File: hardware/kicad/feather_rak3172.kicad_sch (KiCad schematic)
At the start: 49 parts, among them J1 Pin Header, J2 Pin Header, J3 USB_C_Receptacle_USB2.0, J4 915MHz SMA, J5 SWD, J6 JST-2PH, Q1 DMG341, SW1 RESET, SW2 BOOT, U1 RAK3172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

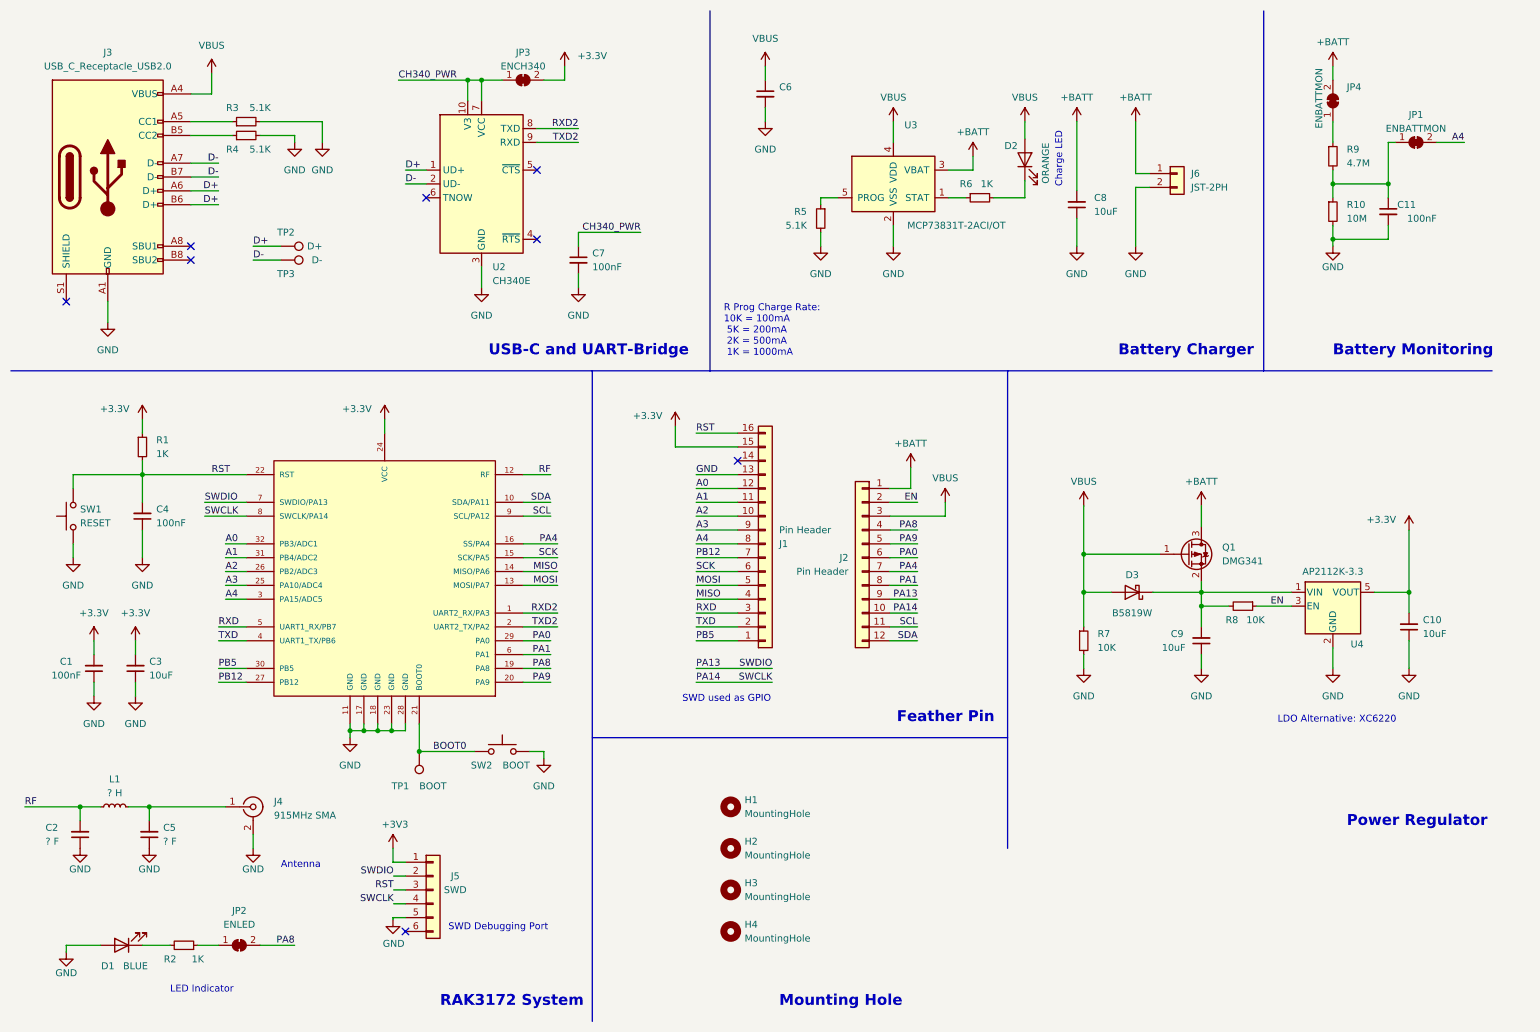
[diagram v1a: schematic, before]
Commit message: remove matching circuit, trace too short
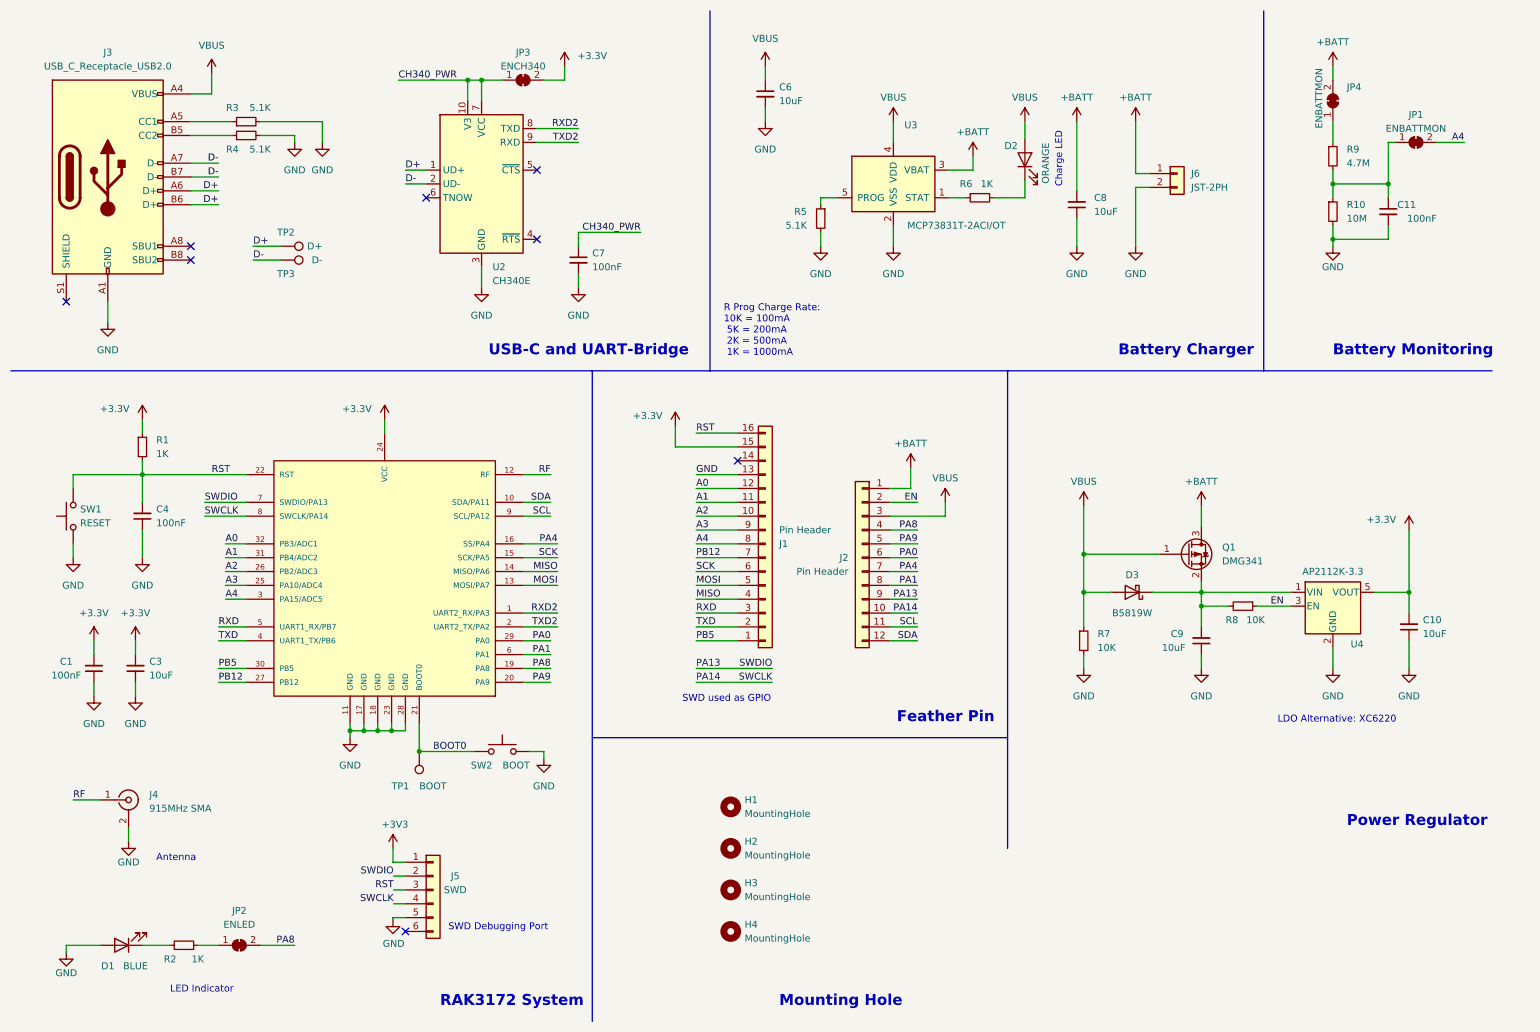
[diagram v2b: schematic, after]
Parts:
- removed C2, C5: ? F, Capacitor_SMD:C_0402_1005Metric, symbol Device:C_Small
- removed L1: ? H, Inductor_SMD:L_0402_1005Metric, symbol Device:L_Small
- C6: value (none) -> 10uF; footprint (none) -> Capacitor_SMD:C_0603_1608Metric
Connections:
- net RF: now also J4.1 (In)
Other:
- moved on the sheet: J4

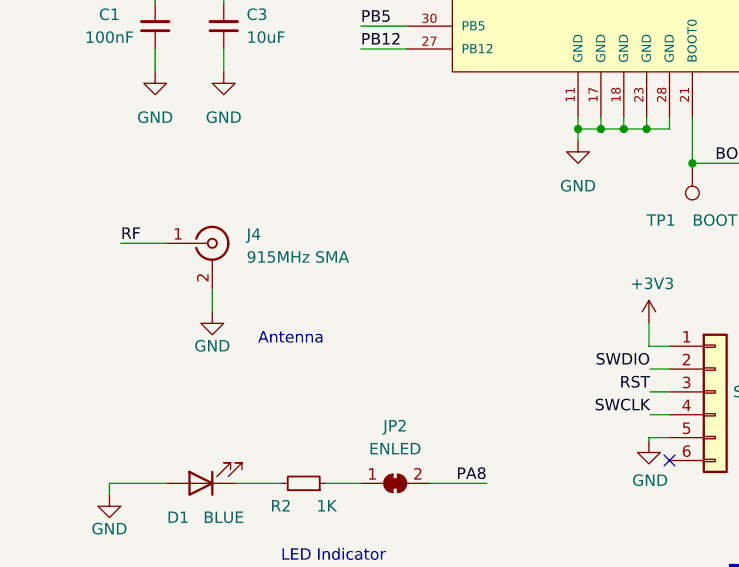
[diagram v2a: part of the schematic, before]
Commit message: re-add matching circuit, improve rf trace angle
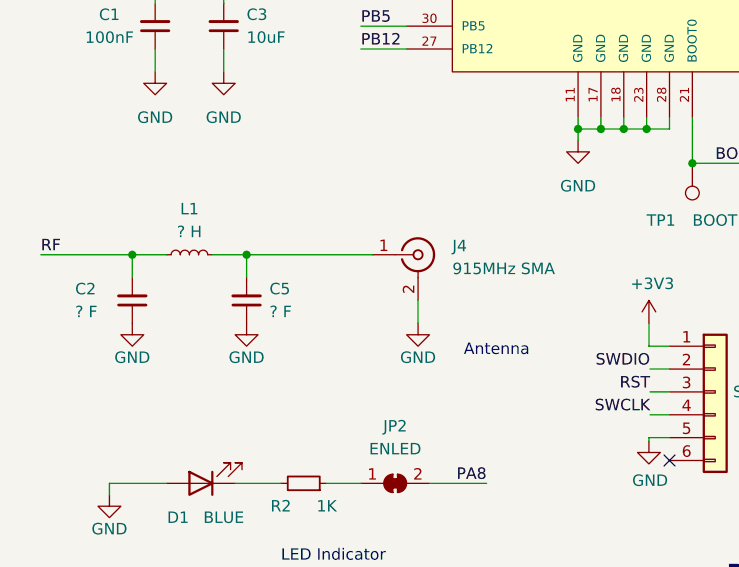
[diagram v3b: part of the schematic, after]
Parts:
- added C2, C5: ? F, Capacitor_SMD:C_0402_1005Metric, symbol Device:C_Small
- added L1: ? H, Inductor_SMD:L_0402_1005Metric, symbol Device:L_Small
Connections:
- net GND: now also C2.1, C5.1
- net RF: now also C2.2, L1.1; no longer J4.1 (In)
- new net: C5.2, J4.1 (In), L1.2
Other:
- moved on the sheet: J4

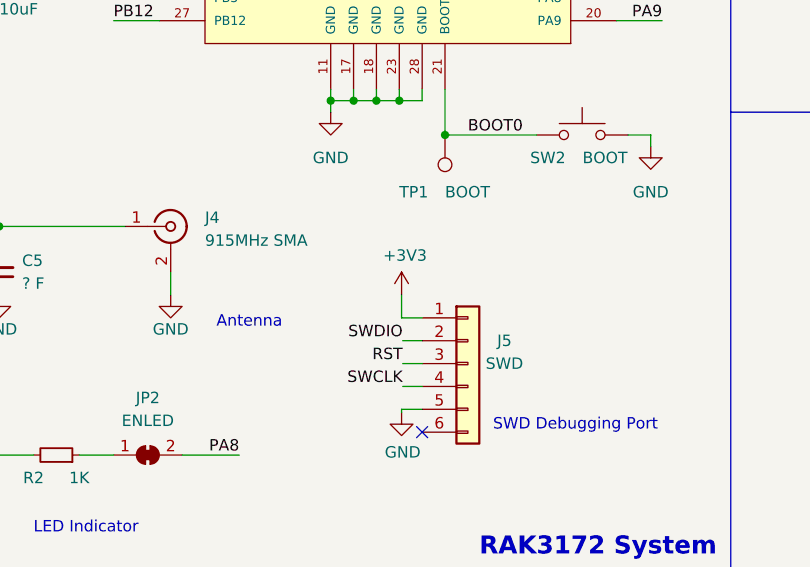
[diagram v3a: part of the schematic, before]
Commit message: remove 3v3 signal from swd pinout
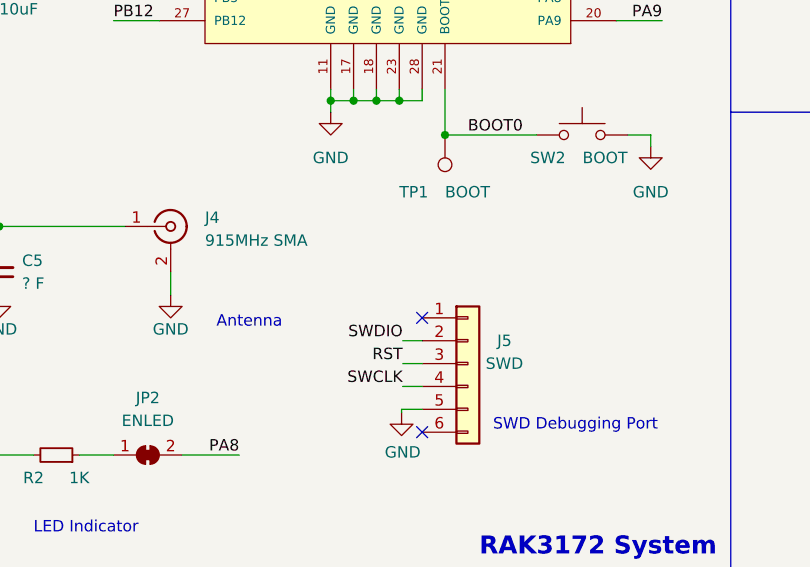
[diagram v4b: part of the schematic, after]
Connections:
- net +3V3: no longer names the net of J5.1 (Pin_1)
- no-connect marks 8 -> 9
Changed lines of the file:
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@@
   (no_connect (at 109.22 41.91))
   (no_connect (at 146.05 95.25))
+  (no_connect (at 85.09 168.91))
   (no_connect (at 88.9 46.99))
   (no_connect (at 22.86 66.04))
@@
     (stroke (width 0) (type default) (color 0 0 0 0))
   )
-  (wire (pts (xy 82.804 168.91) (xy 85.09 168.91))
-    (stroke (width 0) (type default) (color 0 0 0 0))
-  )
   (wire (pts (xy 49.53 27.94) (xy 45.72 27.94))
     (stroke (width 0) (type default) (color 0 0 0 0))
@@
   )
   (wire (pts (xy 138.43 133.35) (xy 152.4 133.35))
-    (stroke (width 0) (type default) (color 0 0 0 0))
-  )
-  (wire (pts (xy 82.804 166.37) (xy 82.804 168.91))
     (stroke (width 0) (type default) (color 0 0 0 0))
   )
@@
     (pin "2")
   )
-  (symbol (lib_id "power:+3V3") (at 82.804 166.37 0) (unit 1)
-    (in_bom yes) (on_board yes)
-    (property "Reference" "#PWR0125" (id 0) (at 82.804 170.18 0)
-      (effects (font (size 1.27 1.27)) hide)
-    )
-    (property "Value" "+3V3" (id 1) (at 83.185 161.9758 0))
-    (property "Footprint" "" (id 2) (at 82.804 166.37 0)
-      (effects (font (size 1.27 1.27)) hide)
-    )
-    (property "Datasheet" "" (id 3) (at 82.804 166.37 0)
-      (effects (font (size 1.27 1.27)) hide)
-    )
-    (pin "1")
-  )
   (symbol (lib_id "Device:R_Small") (at 190.5 46.99 90) (mirror x) (unit 1)
     (in_bom yes) (on_board yes)
@@
       (reference "#PWR0124") (unit 1) (value "GND") (footprint "")
     )
-    (path "/ec477f20-2bfc-47a1-aeed-0615d880ae23"
-      (reference "#PWR0125") (unit 1) (value "+3V3") (footprint "")
-    )
     (path "/799d7101-51e0-4b76-88e0-543d20c53ec5"

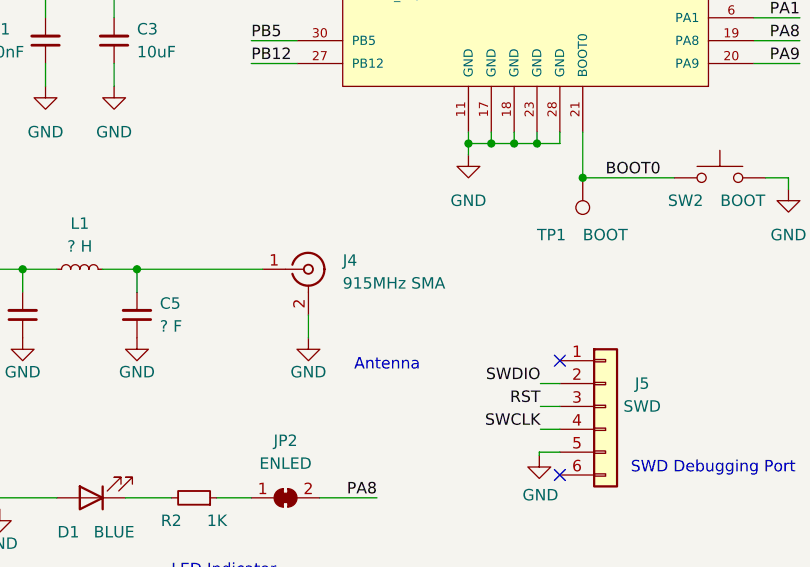
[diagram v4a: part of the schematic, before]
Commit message: change antenna part number
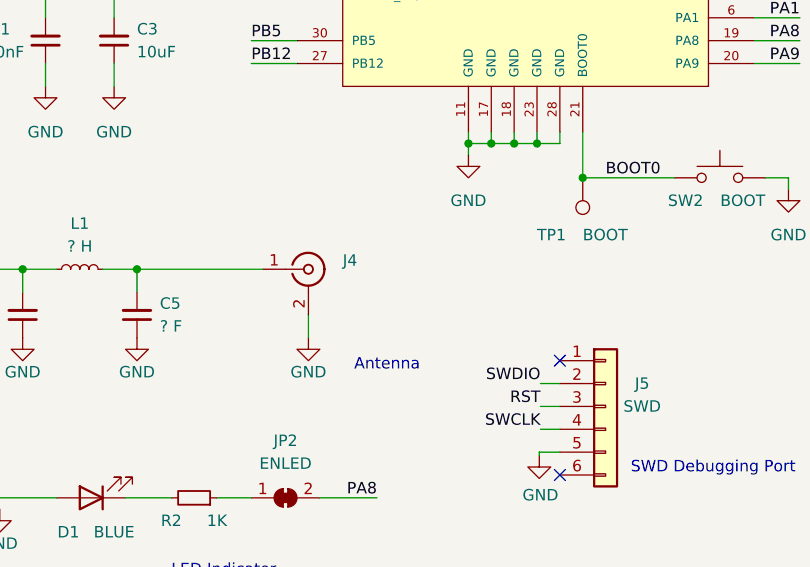
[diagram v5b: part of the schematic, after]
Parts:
- J4: value 915MHz SMA -> (none); footprint Teapot:SMA_HJTech_023 -> (none); Manufacturer HJ Tech -> DreamLNK; Part Number HJ-SMA023 -> SMA-KE-P903
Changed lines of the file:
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@@
       (effects (font (size 1.27 1.27)) (justify left))
     )
-    (property "Value" "915MHz SMA" (id 1) (at 60.96 160.3131 0)
+    (property "Value" "" (id 1) (at 60.96 160.3131 0)
       (effects (font (size 1.27 1.27)) (justify left))
     )
-    (property "Footprint" "Teapot:SMA_HJTech_023" (id 2) (at 57.15 158.75 0)
+    (property "Footprint" "" (id 2) (at 57.15 158.75 0)
       (effects (font (size 1.27 1.27)) hide)
     )
@@
       (effects (font (size 1.27 1.27)) hide)
     )
-    (property "Manufacturer" "HJ Tech" (id 4) (at 57.15 158.75 0)
+    (property "Manufacturer" "DreamLNK" (id 4) (at 57.15 158.75 0)
       (effects (font (size 1.27 1.27)) hide)
     )
-    (property "Part Number" "HJ-SMA023" (id 5) (at 57.15 158.75 0)
+    (property "Part Number" "SMA-KE-P903" (id 5) (at 57.15 158.75 0)
       (effects (font (size 1.27 1.27)) hide)
     )
